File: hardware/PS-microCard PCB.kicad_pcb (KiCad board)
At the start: 4 copper layers, 36.2 x 70.2 mm, 67 parts, among them J1 Oled Socket, J3 MEM2052-00-195-00-A_REVA, J6 JST Debug Connector, SW1 FSM4JSMA, SW2 FSM4JSMA, U1 W25Q128JVS, U2 RP2350_60QFN, U5 TPS7A2033PDBVR, Y1 ABM8-272-T3

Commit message: new pcb revision
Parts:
- removed ?: , 
- removed CMD: PS1_CMD_DBG, TestPoint:TestPoint_Pad_D1.0mm
- removed DATA: PS1_DATA_DBG, TestPoint:TestPoint_Pad_D1.0mm
- removed REF** (x2): Fiducial_1mm_Mask3mm, Fiducial:Fiducial_1mm_Mask3mm
- added C20: 1u, Capacitor_SMD:C_0402_1005Metric, F.Cu at (163.4, 114.6)
- added C21: 1u, Capacitor_SMD:C_0402_1005Metric, F.Cu at (163.6, 108.0)
- added C23: 100n, Capacitor_SMD:C_0402_1005Metric, F.Cu at (166.6, 99.9)
- added C25: 100n, Capacitor_SMD:C_0402_1005Metric, F.Cu at (162.1, 103.1)
- added C28: 100n, Capacitor_SMD:C_0402_1005Metric, F.Cu at (164.7, 103.2)
- added J2: 10118194-0001LF, footprints:AMPHENOL_10118194-0001LF, F.Cu at (164.1, 120.7)
- added R20: 10k, Resistor_SMD:R_0402_1005Metric, F.Cu at (161.8, 92.9)
- added R21: 20k, Resistor_SMD:R_0402_1005Metric, F.Cu at (163.5, 92.4)
- added R6: 27, Resistor_SMD:R_0402_1005Metric, F.Cu at (159.1, 86.7)
- added R7: 27, Resistor_SMD:R_0402_1005Metric, F.Cu at (159.1, 87.8)
- added R9: 700, Resistor_SMD:R_0402_1005Metric, F.Cu at (161.8, 94.0)
- added TP10: PS1_CMD_DBG, TestPoint:TestPoint_Pad_D1.0mm, F.Cu at (146.2, 74.3)
- added TP9: PS1_DATA_DBG, TestPoint:TestPoint_Pad_D1.0mm, F.Cu at (143.8, 74.3)
- added U3: TLV75533PDBVR, footprints:TLV75533PDBVR-SOT95P280X145-5N, F.Cu at (164.1, 111.0)
- added U4: TPS2113APWR, footprints:TPS2113-SOP65P640X120-8N, F.Cu at (163.8, 98.4)
- C16, C8, J3: moved to B.Cu
- C22, C24, R10, R8: moved to F.Cu
- moved C19 33.1 mm to (163.2, 105.1), turned to 180 degrees
- moved R11 29.6 mm to (137.1, 93.4), turned to 180 degrees
- moved J6 29.5 mm to (136.1, 97.8), turned to 90 degrees
- moved S1 28.6 mm to (137.8, 91.5), turned to 0 degrees
- moved J1 21.8 mm to (157.5, 99.5)
- moved C24 21.1 mm to (153.8, 114.0), turned to 0 degrees
- moved C22 17.8 mm to (153.1, 115.8), turned to 0 degrees
- moved J3 13.0 mm to (151.1, 115.1), turned to 180 degrees
- moved R8 12.3 mm to (149.8, 115.9), turned to 180 degrees
- moved SW1 8.97 mm to (138.4, 110.9)
- moved R17 8.95 mm to (140.7, 103.7)
- moved SW2 7.77 mm to (164.1, 110.9)
- moved TP13 7.61 mm to (158.7, 74.7)
- moved C27 6.45 mm to (151.1, 71.2), turned to 180 degrees
- moved C26 6.18 mm to (152.0, 77.8)
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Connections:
- C26 pad 1: +3V3 -> /PS1_3V3
- S1 pad 1: /RUN -> unconnected-(S1-Pad1)
- S1 pad 4: Net-(R11-Pad2) -> unconnected-(S1-Pad4)
- S2 pad 2: GND -> unconnected-(S2-Pad2)
- S2 pad 3: /USB_BOOT -> unconnected-(S2-Pad3)
- SW1 pad 2: GND -> unconnected-(SW1-Pad2)
- SW1 pad 4: Net-(R17-Pad1) -> unconnected-(SW1-Pad4)
- SW2 pad 1: GND -> Net-(R18-Pad1)
- SW2 pad 2: GND -> unconnected-(SW2-Pad2)
- SW2 pad 3: Net-(R18-Pad1) -> GND
- SW2 pad 4: Net-(R18-Pad1) -> unconnected-(SW2-Pad4)
- U2 pad 12: /Left Button -> unconnected-(U2-GPIO8-Pad12)
- U2 pad 13: /Right Button -> unconnected-(U2-GPIO9-Pad13)
- U2 pad 31: unconnected-(U2-GPIO19-Pad31) -> /Right Button
- U2 pad 43: unconnected-(U2-GPIO29_ADC3-Pad43) -> /Left Button
- U2 pad 51: unconnected-(U2-USB_DM-Pad51) -> /D-
- U2 pad 52: unconnected-(U2-USB_DP-Pad52) -> /D+
- U5 pad 5: +3V3 -> /PS1_3V3
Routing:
- net /OLED_CS: track 90.2 -> 35.6 mm
- net /OLED_D/C: track 87.5 -> 36.5 mm, vias 0 -> 2
- net /PS1_3V3: track 0.00 -> 37.4 mm, vias 0 -> 2
- net Net-(J2-D+): track 0.00 -> 34.9 mm, vias 0 -> 2
- net /Left Button: track 51.0 -> 17.4 mm
- net Net-(J2-D-): track 0.00 -> 32.6 mm, vias 0 -> 2
- net /OLED_MOSI: track 73.3 -> 43.7 mm
- net /SD_MISO: track 17.2 -> 44.3 mm, vias 0 -> 1
- net /Right Button: track 42.7 -> 15.6 mm
- net /SWD: track 37.3 -> 14.3 mm
- net /RUN: track 31.4 -> 9.73 mm, vias 2 -> 0
- net /OLED_SCK: track 68.8 -> 49.0 mm
- net /SWCLK: track 34.9 -> 17.2 mm
- net GND: track 77.0 -> 61.1 mm, vias 41 -> 54
- net /SD_MOSI: track 24.0 -> 38.8 mm, vias 2 -> 1
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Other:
- board text removed: "ACK"
- board text removed: "CS"
- board text removed: "SCK"

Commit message: Revision 1.0A finished
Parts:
- removed U5: TPS7A2033PDBVR, footprints:TPS7A2033PDBVR-SOT95P280X145-5N
- added C29: 220n, Capacitor_SMD:C_0402_1005Metric, B.Cu at (157.6, 94.7)
- added C30: 220n, Capacitor_SMD:C_0402_1005Metric, F.Cu at (157.6, 98.4)
- added C31: 4.7u, Capacitor_SMD:C_0402_1005Metric, F.Cu at (155.1, 98.8)
- added C32: 4.7u, Capacitor_SMD:C_0402_1005Metric, F.Cu at (145.3, 98.9)
- added C33: 4.7u, Capacitor_SMD:C_0402_1005Metric, F.Cu at (154.1, 98.8)
- added C34: 4.7u, Capacitor_SMD:C_0402_1005Metric, F.Cu at (144.3, 98.9)
- added C35: 10u, Capacitor_SMD:C_0402_1005Metric, F.Cu at (139.5, 110.5)
- added C36: 10u, Capacitor_SMD:C_0402_1005Metric, F.Cu at (138.0, 104.5)
- added L2: 4.7u, Inductor_SMD:L_Bourns-SRN4018, F.Cu at (136.9, 113.5)
- added R22: 267k, Resistor_SMD:R_0402_1005Metric, F.Cu at (146.4, 98.9)
- added R23: 10k, Resistor_SMD:R_0402_1005Metric, F.Cu at (152.7, 98.8)
- added R24: 10k, Resistor_SMD:R_0402_1005Metric, F.Cu at (151.6, 98.8)
- added R25: 214k, Resistor_SMD:R_0402_1005Metric, F.Cu at (138.0, 105.9)
- added R26: 100k, Resistor_SMD:R_0402_1005Metric, F.Cu at (140.1, 105.9)
- added R27: 100k, Resistor_SMD:R_0402_1005Metric, F.Cu at (150.1, 75.8)
- added R28: 20k, Resistor_SMD:R_0402_1005Metric, F.Cu at (149.1, 77.0)
- added TP14: SD_SCK, TestPoint:TestPoint_Pad_D1.0mm, B.Cu at (155.8, 104.1)
- added TP15: SD_MISO, TestPoint:TestPoint_Pad_D1.0mm, B.Cu at (157.9, 104.1)
- added TP16: SD_CS, TestPoint:TestPoint_Pad_D1.0mm, B.Cu at (147.2, 105.0)
- added TP17: SD_DETECT, TestPoint:TestPoint_Pad_D1.0mm, B.Cu at (153.6, 104.1)
- added TP18: SD_MOSI, TestPoint:TestPoint_Pad_D1.0mm, B.Cu at (144.4, 105.0)
- added U6: MCP1640BT-I_CHY, footprints:SOT95P280X145-6N, F.Cu at (136.9, 109.2)
- added U7: TLV75801PDBVR, footprints:SOT95P280X145-5N, F.Cu at (150.6, 72.8)
- C27: value 1u -> 10u
- J1: value Oled Socket -> FH12-30S-0.5SH_55_; footprint Connector_PinSocket_2.54mm:PinSocket_1x06_P2.54mm_Vertical -> footprints:HIROSE_FH12-30S-0.5SH_55_
- R11: value 1K -> 1k
- R21: value 20k -> 28.7k
- moved J1 7.25 mm to (151.0, 96.3), turned to 180 degrees
- moved C23 2.09 mm to (165.0, 101.2), turned to 90 degrees
- moved C26 1.93 mm to (152.1, 75.8)
- moved U3 1.54 mm to (162.8, 111.9)
- moved R20 1.54 mm to (160.6, 93.8)
- moved U4 1.54 mm to (162.6, 99.3)
- moved C19 1.54 mm to (162.0, 106.0)
- moved C20 1.54 mm to (162.2, 115.5)
- moved C25 1.54 mm to (160.9, 104.0)
- moved C21 1.54 mm to (162.4, 108.9)
- moved C28 1.54 mm to (163.4, 104.1)
- moved R21 1.54 mm to (162.3, 93.3)
- moved R9 1.54 mm to (160.5, 94.9)
- moved C27 1.26 mm to (151.1, 69.9)
- moved J2 0.18 mm to (164.1, 120.5)
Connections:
- net Net-(J2-D+) renamed /DIFF+
- net Net-(J2-D-) renamed /DIFF-
- J1 pad 1: +3V3 -> unconnected-(J1-NC_GND-Pad1)
- J1 pad 2: GND -> Net-(J1-C1N)
- J1 pad 3: /OLED_SCK -> Net-(J1-C1P)
- J1 pad 4: /OLED_MOSI -> Net-(J1-C2P)
- J1 pad 5: /OLED_D/C -> Net-(J1-C2N)
- J1 pad 6: /OLED_CS -> /OLED_3V8
- U2 pad 13: unconnected-(U2-GPIO9-Pad13) -> /OLED_RES
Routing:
- net /OLED_RES: track 0.00 -> 40.1 mm, vias 0 -> 3
- net /OLED_3V8: track 0.00 -> 31.9 mm, vias 0 -> 2
- net /OLED_SCK: track 49.0 -> 24.6 mm, vias 0 -> 1
- net GND: track 61.1 -> 83.0 mm, vias 54 -> 63
- net /OLED_D/C: track 36.5 -> 18.2 mm, vias 2 -> 1
- net /OLED_MOSI: track 43.7 -> 25.7 mm, vias 0 -> 1
- net /OLED_CS: track 35.6 -> 19.1 mm, vias 0 -> 2
- net /SWCLK: track 17.2 -> 26.2 mm
- net /SD_MISO: track 44.3 -> 36.0 mm
- net /SWD: track 14.3 -> 21.5 mm
- net /PS1_3V3: track 37.4 -> 40.9 mm
- net Net-(U6-VFB): track 0.00 -> 3.26 mm
- net Net-(J1-C2P): track 0.00 -> 3.12 mm, vias 0 -> 1
- net +3V3: track 46.9 -> 50.0 mm, vias 12 -> 15
- net Net-(U7-FB): track 0.00 -> 2.78 mm
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- added copper zone on F.Cu, net Net-(U6-SW)

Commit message: Hardware revision 1.1A
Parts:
- removed C19: 10u, Capacitor_SMD:C_0805_2012Metric
- removed C26: 4.7u, Capacitor_SMD:C_0402_1005Metric
- removed C27: 10u, Capacitor_SMD:C_0402_1005Metric
- removed C28: 100n, Capacitor_SMD:C_0402_1005Metric
- removed R20: 10k, Resistor_SMD:R_0402_1005Metric
- removed R21: 28.7k, Resistor_SMD:R_0402_1005Metric
- removed R9: 700, Resistor_SMD:R_0402_1005Metric
- removed U4: TPS2113APWR, footprints:TPS2113-SOP65P640X120-8N
- removed U7: TLV75801PDBVR, footprints:SOT95P280X145-5N
- added C37: 100n, Capacitor_SMD:C_0402_1005Metric_Pad0.74x0.62mm_HandSolder, F.Cu at (161.5, 98.8)
- added C38: 1u, Capacitor_SMD:C_0402_1005Metric_Pad0.74x0.62mm_HandSolder, F.Cu at (164.2, 94.5)
- added C39: 1u, Capacitor_SMD:C_0402_1005Metric_Pad0.74x0.62mm_HandSolder, F.Cu at (164.6, 96.2)
- added L3: 2.2u, footprints:IND_LQH3NPN2R2MMEL, F.Cu at (160.7, 114.8)
- added R29: 100, Resistor_SMD:R_0402_1005Metric_Pad0.72x0.64mm_HandSolder, F.Cu at (160.9, 104.8)
- added R30: 0, Resistor_SMD:R_0402_1005Metric_Pad0.72x0.64mm_HandSolder, F.Cu at (158.6, 107.1)
- added R31: 0, Resistor_SMD:R_0402_1005Metric_Pad0.72x0.64mm_HandSolder, F.Cu at (157.9, 105.3)
- added U5: TPS63001DRCT, footprints:TPS63001DRCT, F.Cu at (162.0, 111.0)
- C10, C11, C12, C13, C14, C15, C16, C17, C18, C2, C22, C29, C3, C30, C31, C32, C33, C34, C5, C6, C7, C8, C9: footprint Capacitor_SMD:C_0402_1005Metric -> Capacitor_SMD:C_0402_1005Metric_Pad0.74x0.62mm_HandSolder
- C20: value 1u -> 10u; footprint Capacitor_SMD:C_0402_1005Metric -> Capacitor_SMD:C_0805_2012Metric_Pad1.18x1.45mm_HandSolder
- C21: value 1u -> 100n; footprint Capacitor_SMD:C_0402_1005Metric -> Capacitor_SMD:C_0402_1005Metric_Pad0.74x0.62mm_HandSolder
- C23, C25: value 100n -> 10u; footprint Capacitor_SMD:C_0402_1005Metric -> Capacitor_SMD:C_0805_2012Metric_Pad1.18x1.45mm_HandSolder
- C24: footprint Capacitor_SMD:C_0805_2012Metric -> Capacitor_SMD:C_0402_1005Metric_Pad0.74x0.62mm_HandSolder
- C35, C36: footprint Capacitor_SMD:C_0402_1005Metric -> Capacitor_SMD:C_0805_2012Metric_Pad1.18x1.45mm_HandSolder
- L2: footprint Inductor_SMD:L_Bourns-SRN4018 -> Inductor_SMD:L_APV_ANR4018
- R10, R11, R12, R13, R14, R15, R16, R17, R18, R19, R2, R22, R23, R24, R25, R26, R4, R5, R6, R7, R8: footprint Resistor_SMD:R_0402_1005Metric -> Resistor_SMD:R_0402_1005Metric_Pad0.72x0.64mm_HandSolder
- R27: value 100k -> 28.7k; footprint Resistor_SMD:R_0402_1005Metric -> Resistor_SMD:R_0402_1005Metric_Pad0.72x0.64mm_HandSolder
- R28: value 20k -> 10k; footprint Resistor_SMD:R_0402_1005Metric -> Resistor_SMD:R_0402_1005Metric_Pad0.72x0.64mm_HandSolder
- U1: value W25Q128JVS -> S25FL128LAGMFI010
- U3: value TLV75533PDBVR -> TPS2116DRLR; footprint footprints:TLV75533PDBVR-SOT95P280X145-5N -> footprints:TPS2116DRLR
- moved R27 27.8 mm to (163.5, 100.2), turned to 90 degrees
- moved R28 26.2 mm to (164.2, 98.3)
- moved U3 15.6 mm to (162.6, 96.3)
- moved C23 12.5 mm to (156.7, 110.6)
- moved C25 6.86 mm to (158.8, 110.5), turned to 90 degrees
- moved C20 6.72 mm to (165.1, 109.5), turned to 90 degrees
- moved C24 1.94 mm to (151.9, 114.7), turned to 180 degrees
- moved R26 1.55 mm to (141.6, 106.0)
- moved C21 1.32 mm to (163.0, 107.8), turned to 90 degrees
- moved R25 1.23 mm to (139.2, 106.0)
- moved C36 1.16 mm to (136.8, 104.8), turned to -90 degrees
- moved C35 0.83 mm to (140.2, 110.2)
- moved C30 0.43 mm to (157.2, 98.4)
- moved C7 0.39 mm to (146.2, 91.0)
- moved C29 0.20 mm to (157.3, 94.6)
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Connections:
- C20 pad 1: Net-(J2-VCC) -> /V_SYS
- C21 pad 1: GND -> Net-(U5-EN)
- C21 pad 2: /USB_3V3 -> GND
- C23 pad 1: GND -> +3V3
- C23 pad 2: /PS1_3V3 -> GND
- C25 pad 1: /USB_3V3 -> +3V3
- J2 pad 1: Net-(J2-VCC) -> /USB_5V
- R27 pad 1: /PS1_3V3 -> /USB_5V
- R27 pad 2: Net-(U7-FB) -> Net-(U3-PR1)
- R28 pad 1: GND -> Net-(U3-PR1)
- R28 pad 2: Net-(U7-FB) -> GND
- U3 pad 1: Net-(J2-VCC) -> GND
- U3 pad 2: GND -> /V_SYS
- U3 pad 3: Net-(J2-VCC) -> /USB_5V
- U3 pad 4: (no net) -> Net-(U3-PR1)
- U3 pad 5: /USB_3V3 -> /USB_5V
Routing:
- net /PS1_3V5: track 0.00 -> 43.5 mm, vias 0 -> 2
- net /PS1_3V3: track 40.9 -> 0.00 mm, vias 2 -> 0
- net /USB_5V: track 0.00 -> 27.0 mm
- net /V_SYS: track 0.00 -> 17.5 mm
- net Net-(U5-EN): track 0.00 -> 11.4 mm, vias 0 -> 2
- net /USB_3V3: track 9.05 -> 0.00 mm
- net Net-(J2-VCC): track 8.38 -> 0.00 mm
- net Net-(U5-PS/SYNC): track 0.00 -> 6.69 mm
- net +3V3: track 50.0 -> 44.1 mm, vias 15 -> 16
- net Net-(U4-VSNS): track 3.74 -> 0.00 mm
- net GND: track 83.0 -> 79.5 mm, vias 63 -> 57
- net Net-(U7-FB): track 2.78 -> 0.00 mm
- net Net-(U3-PR1): track 0.00 -> 2.58 mm
- net Net-(U4-ILIM): track 1.82 -> 0.00 mm
- net /OLED_3V8: track 31.9 -> 33.3 mm
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- added copper zone on F.Cu, net /V_SYS
- added copper zone on F.Cu, net Net-(U5-L1)
- added copper zone on F.Cu, net Net-(U5-L2)
- removed copper zone on F.Cu, net /PS1_3V5

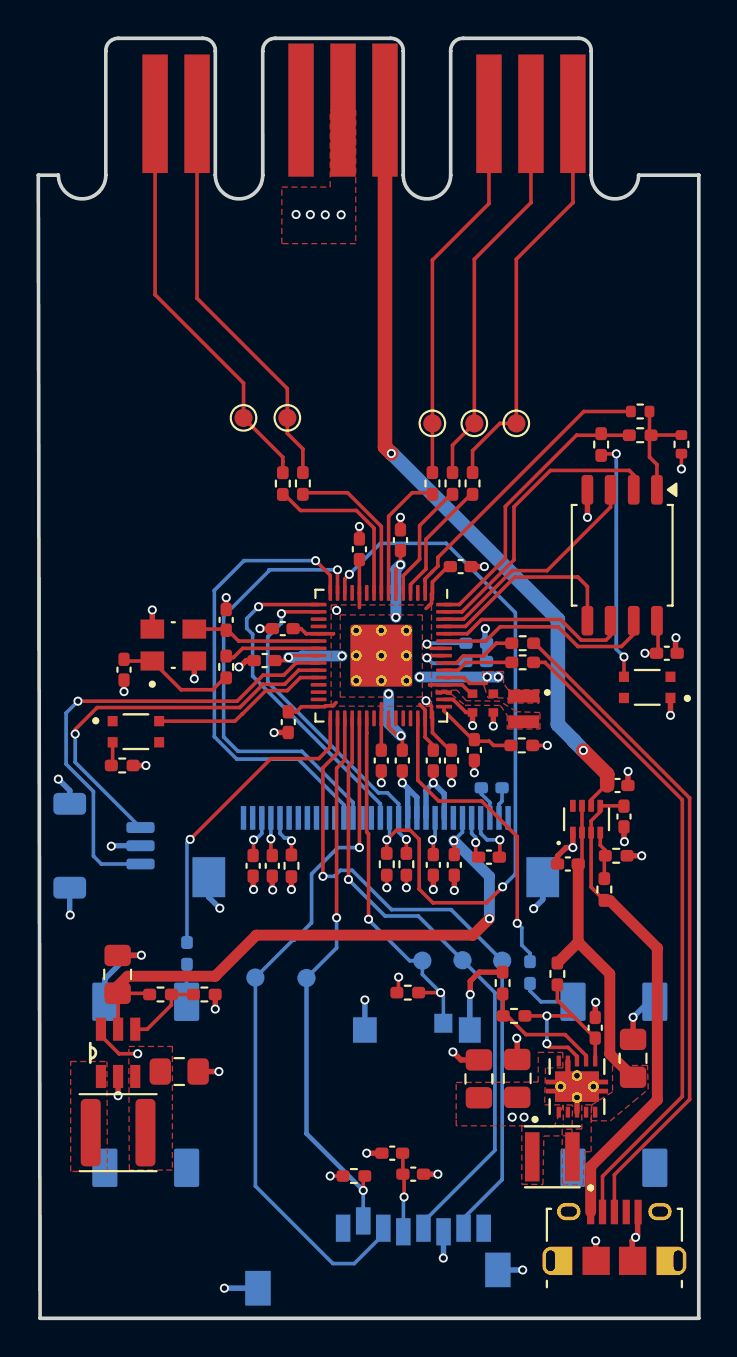
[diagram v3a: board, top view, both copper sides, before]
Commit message: Fix for pcbway and little cleanup
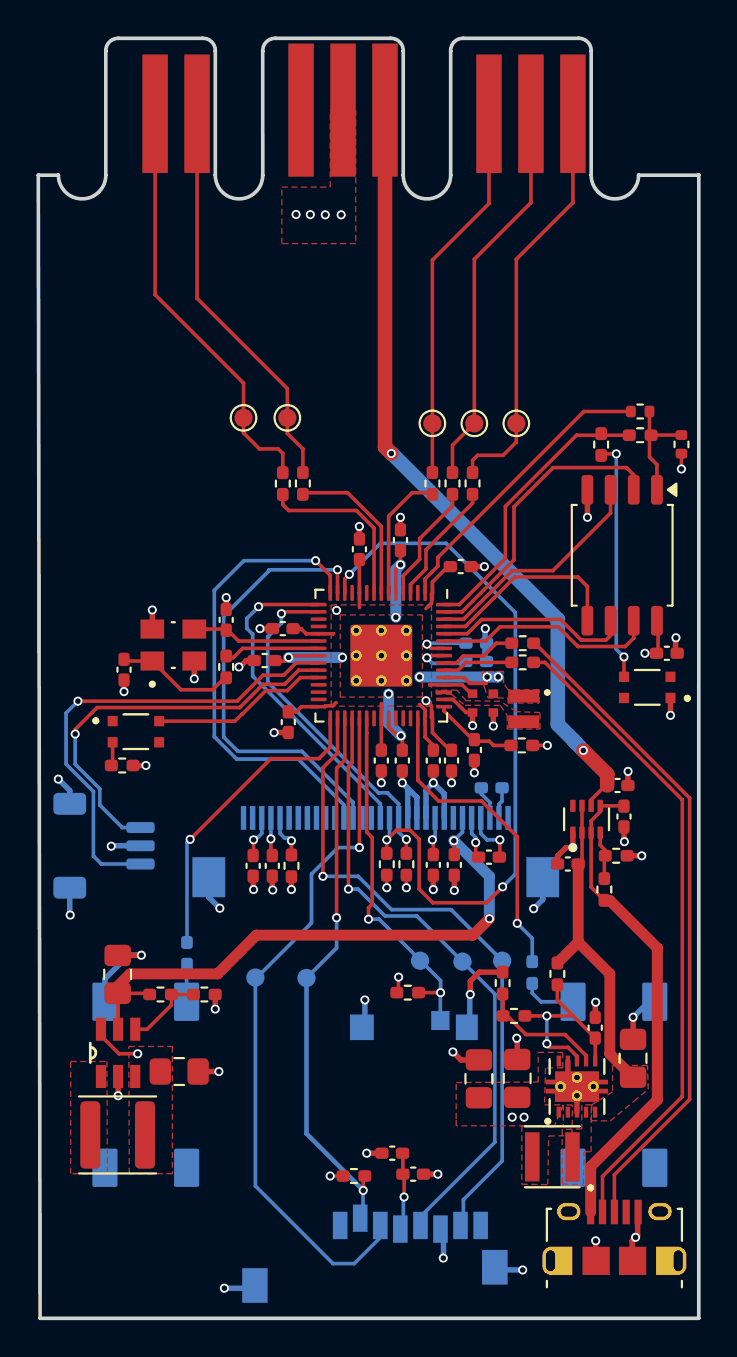
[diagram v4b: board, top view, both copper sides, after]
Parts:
- R1, R3: value DNF -> 0
- R25: value 214k -> 215k
- moved J3 0.22 mm to (150.9, 115.0)
- moved L2 0.13 mm to (136.8, 113.7)
- moved R18 0.12 mm to (159.6, 104.8)
- moved TP17 0.12 mm to (153.4, 104.1)
- moved TP14 0.08 mm to (155.8, 104.2)
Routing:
- net Net-(U5-L2): track 0.81 -> 0.00 mm
- net /PS1_DATA_DBG: track 22.7 -> 23.3 mm
- net /SWD: track 21.5 -> 22.1 mm
- net /SD_SCK: track 33.7 -> 34.2 mm
